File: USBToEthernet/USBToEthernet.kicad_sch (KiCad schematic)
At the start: 14 parts, among them J1 USB_A, J3 RJMG1S8008101BR, U1 LAN7500-ABJZ, U2 NCP1117-3.3_SOT223, U3 93LCxxAxxOT, U4 USBLC6-2SC6, U6 AMS1117-1.2, Y1 25Mhz

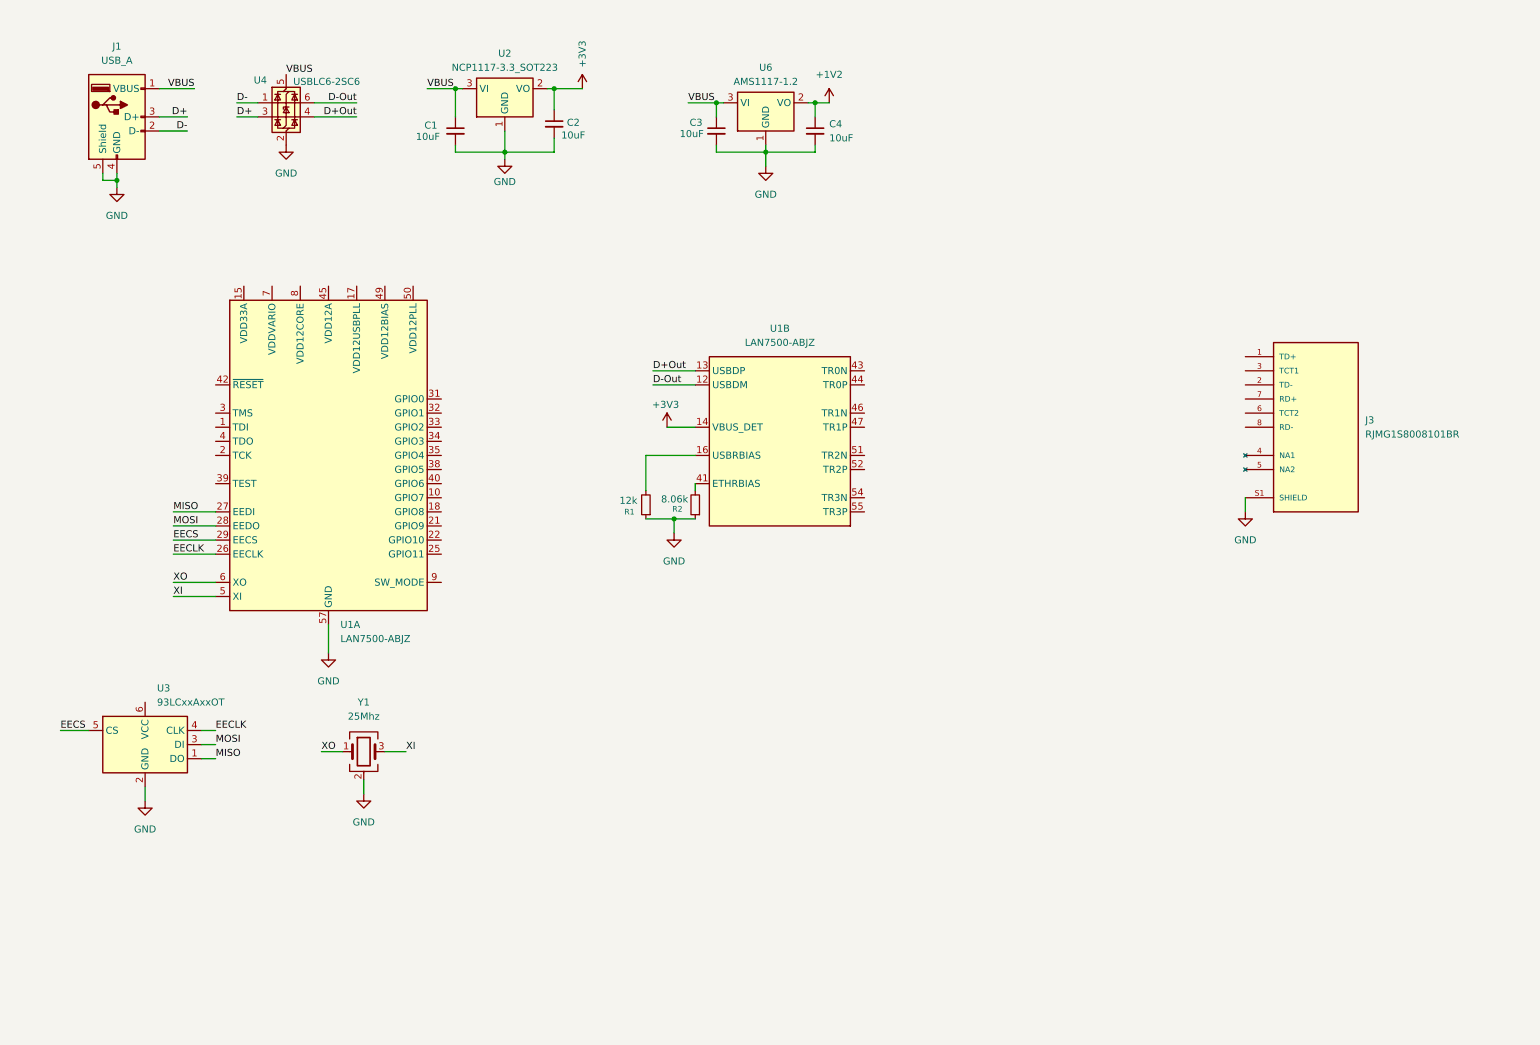
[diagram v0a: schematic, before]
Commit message: Added library for RJ45
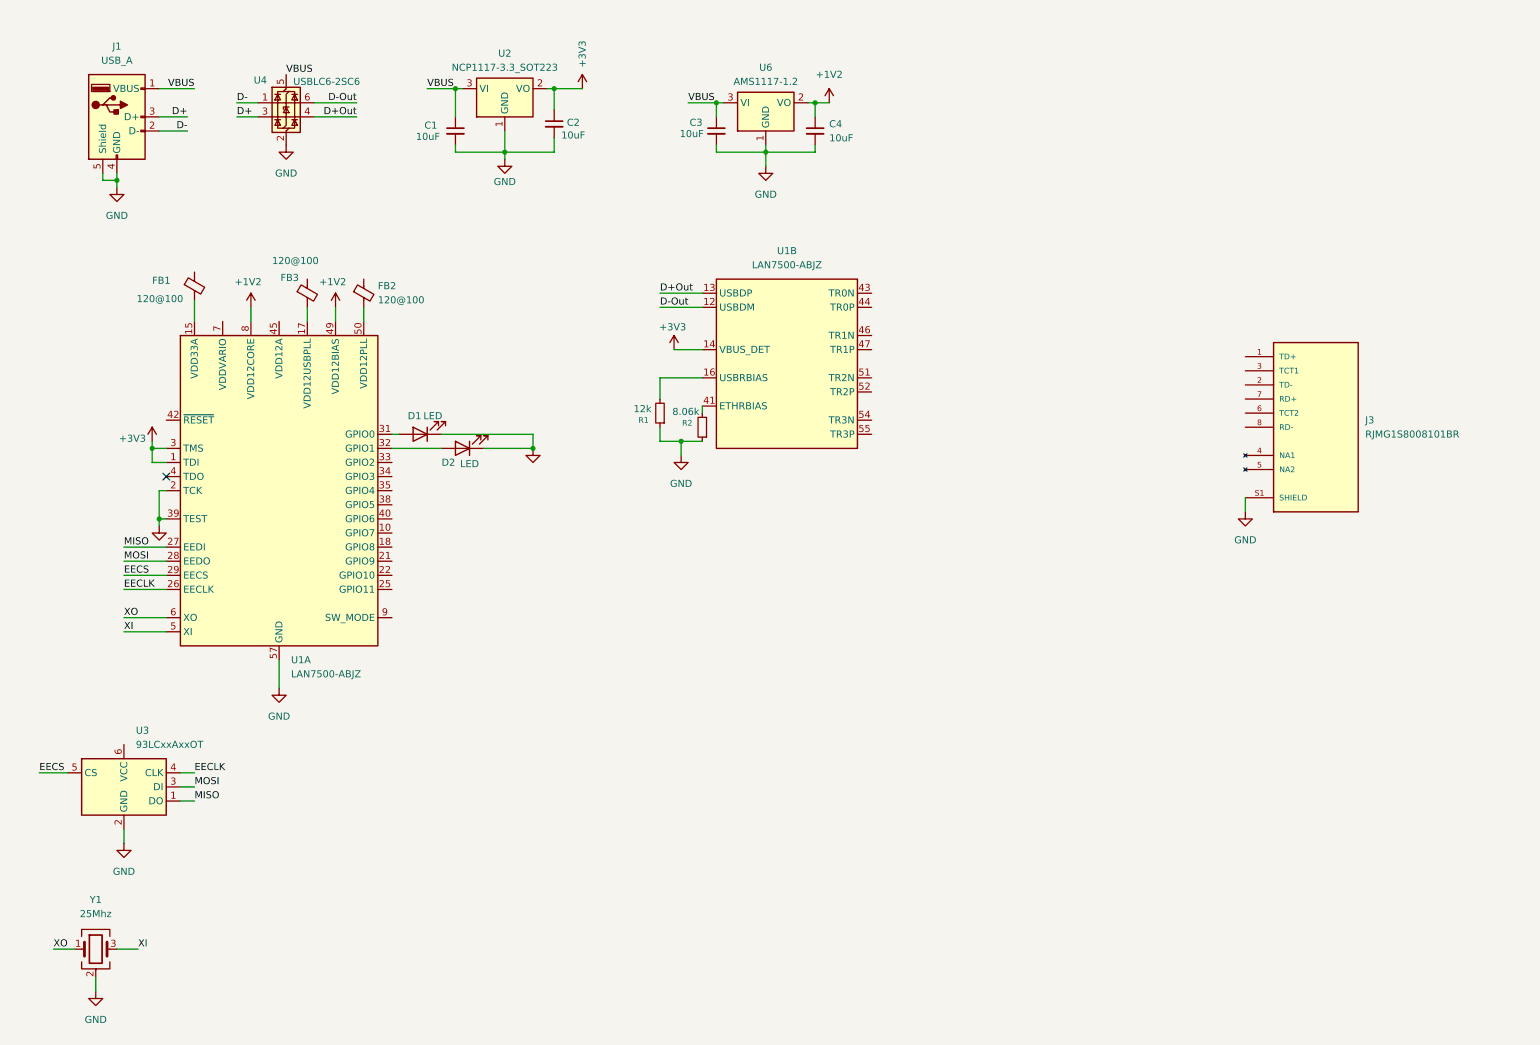
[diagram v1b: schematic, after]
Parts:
- added D1, D2: LED, symbol Device:LED
- added FB1, FB2, FB3: 120@100, symbol Device:FerriteBead_Small
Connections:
- net +1V2: now also U1.11 (VDD12CORE), U1.20 (VDD12CORE), U1.23 (VDD12CORE), U1.30 (VDD12CORE), U1.36 (VDD12CORE), U1.49 (VDD12BIAS), U1.8 (VDD12CORE)
- net +3V3: now also U1.1 (TDI), U1.3 (TMS)
- net GND: now also U1.2 (TCK), U1.39 (TEST), D1.1 (K), D2.1 (K)
- net at U1.15 (VDD33A): now also FB1.2
- net at U1.17 (VDD12USBPLL): now also FB3.2
- net at U1.31 (GPIO0): now also D1.2 (A)
- net at U1.32 (GPIO1): now also D2.2 (A)
- net at U1.50 (VDD12PLL): now also FB2.2
- no-connect marks 0 -> 1
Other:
- moved on the sheet: R1, R2, U1A, U1B, U3, Y1

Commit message: Finished wiring RJ45 and most of LAN7500
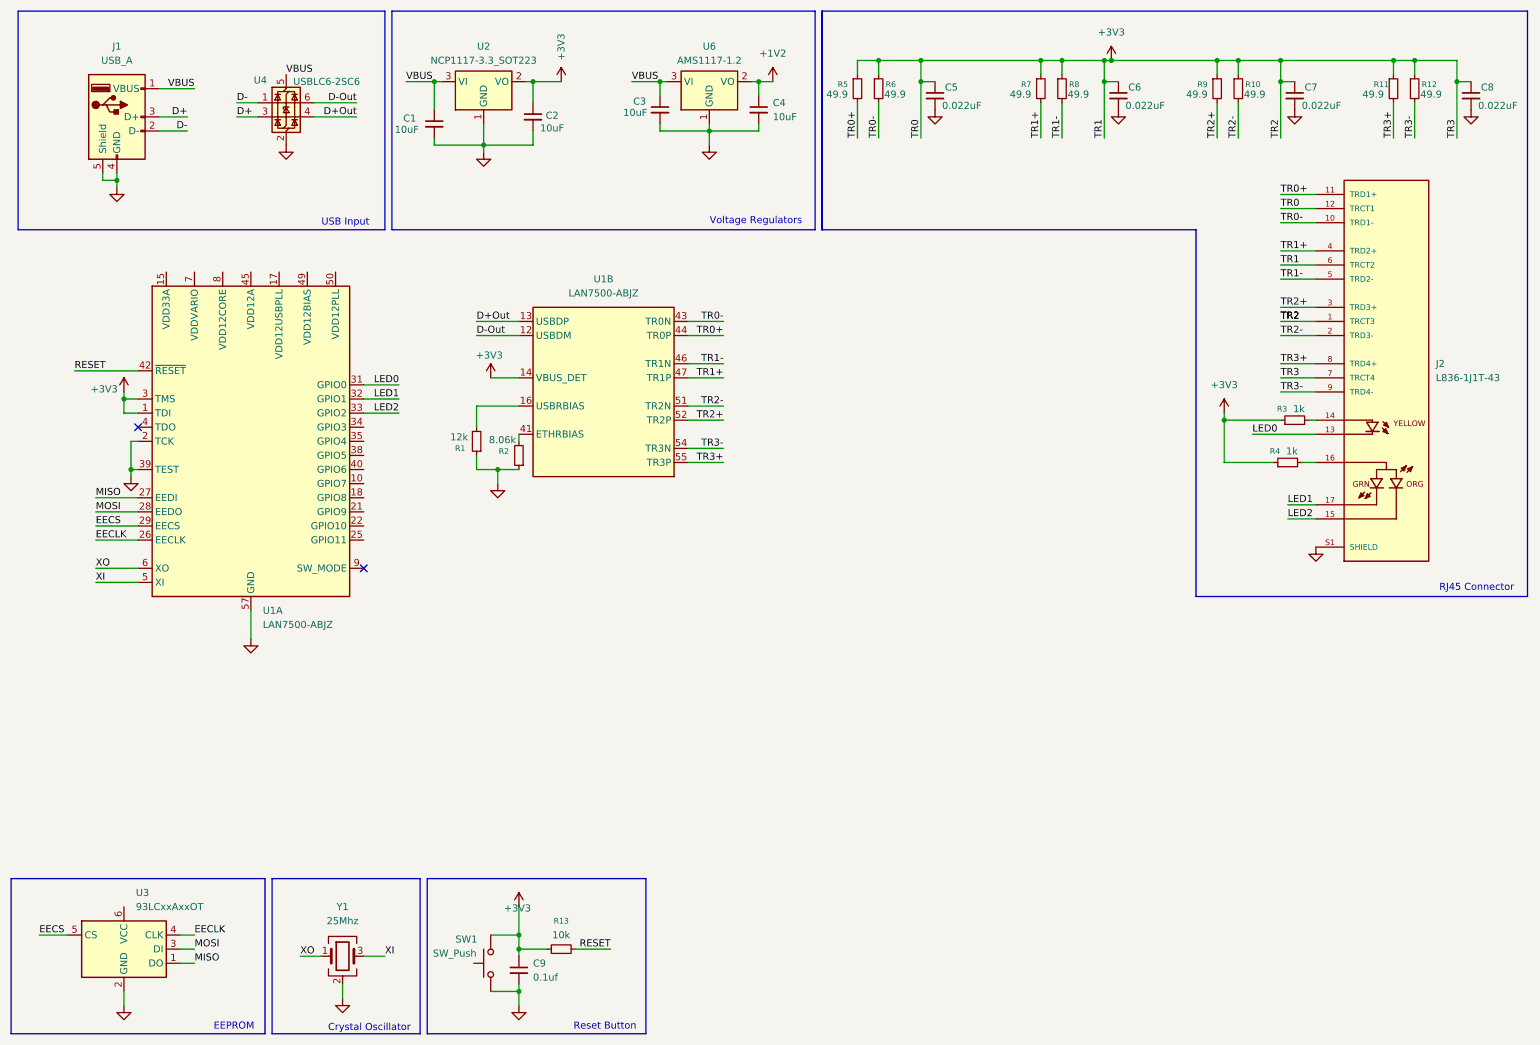
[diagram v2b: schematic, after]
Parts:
- removed D1, D2: LED, symbol Device:LED
- removed FB1, FB2, FB3: 120@100, symbol Device:FerriteBead_Small
- removed J3: RJMG1S8008101BR, RJMG1S8008101BR:AMPHENOL_RJMG1S8008101BR, symbol RJMG1S8008101BR:RJMG1S8008101BR
- added C5, C6, C7, C8: 0.022uF, symbol Device:C_Small
- added C9: 0.1uf, symbol Device:C_Small
- added J2: L836-1J1T-43, L836-1J1T-43:BEL_L836-1J1T-43, symbol L836-1J1T-43:L836-1J1T-43
- added R10, R11, R12, R5, R6, R7, R8, R9: 49.9, Resistor_SMD:R_0201_0603Metric, symbol Device:R_Small
- added R13: 10k, symbol Device:R_Small
- added R3, R4: 1k, symbol Device:R_Small
- added SW1: SW_Push, symbol Switch:SW_Push
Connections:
- net +1V2: no longer U1.11 (VDD12CORE), U1.20 (VDD12CORE), U1.23 (VDD12CORE), U1.30 (VDD12CORE), U1.36 (VDD12CORE), U1.49 (VDD12BIAS), U1.8 (VDD12CORE)
- net +3V3: now also C5.1, C6.1, C7.1, C8.1, C9.1, J2.1 (TRCT3), J2.12 (TRCT1), J2.6 (TRCT2), J2.7 (TRCT4), R10.1, R11.1, R12.1, R13.1, R3.1, R4.1, R5.1, R6.1, R7.1, R8.1, R9.1, SW1.2
- net GND: now also C5.2, C6.2, C7.2, C8.2, C9.2, J2.S1 (SHIELD), J2.S2 (SHIELD), SW1.1
- net TR0-: now reaches U1.43 (TR0N)
- net TR0-: now also J2.10 (TRD1-), R6.2
- net TR0+: now reaches U1.44 (TR0P)
- net TR0+: now also J2.11 (TRD1+), R5.2
- net TR1-: now reaches U1.46 (TR1N)
- net TR1-: now also J2.5 (TRD2-), R8.2
- net TR1+: now reaches U1.47 (TR1P)
- net TR1+: now also J2.4 (TRD2+), R7.2
- net TR2-: now reaches U1.51 (TR2N)
- net TR2-: now also J2.2 (TRD3-), R10.2
- net TR2+: now reaches U1.52 (TR2P)
- net TR2+: now also J2.3 (TRD3+), R9.2
- net TR3-: now reaches U1.54 (TR3N)
- net TR3-: now also J2.9 (TRD4-), R12.2
- net TR3+: now reaches U1.55 (TR3P)
- net TR3+: now also J2.8 (TRD4+), R11.2
- net LED0: now reaches U1.31 (GPIO0)
- net LED0: now also J2.13
- net LED1: now reaches U1.32 (GPIO1)
- net LED1: now also J2.17
- net LED2: now reaches U1.33 (GPIO2)
- net LED2: now also J2.15
- net RESET: now reaches U1.42 (~{RESET})
- net RESET: now also R13.2
- new net: U1.11 (VDD12CORE), U1.20 (VDD12CORE), U1.23 (VDD12CORE), U1.30 (VDD12CORE), U1.36 (VDD12CORE), U1.8 (VDD12CORE)
- new net: J2.14, R3.2
- new net: J2.16, R4.2
- no-connect marks 1 -> 2
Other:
- note added: "Crystal Oscillator"
- note added: "EEPROM"
- note added: "RJ45 Connector"
- note added: "Reset Button"
- note added: "USB Input"
- note added: "Voltage Regulators"
- moved on the sheet: C1, C2, C3, C4, R1, R2, U1A, U1B, U2, U3, U6, Y1

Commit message: Finished schematic
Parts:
- added C10, C11, C12, C13, C14, C15, C16, C17, C18, C20, C21, C22, C23, C24, C25: 1uF, Capacitor_SMD:C_0603_1608Metric, symbol Device:C_Small
- added C19: 100nF, Capacitor_SMD:C_0603_1608Metric, symbol Device:C_Small
- added D1: PTVS10VZ1USK, Diode_SMD:Nexperia_DSN1608-2_1.6x0.8mm, symbol Diode:PTVS10VZ1USK
- added FB1, FB2, FB3, FB4, FB5: 120@100, Inductor_SMD:L_0603_1608Metric, symbol Device:FerriteBead_Small
- C1, C2, C3, C4, C5, C6, C7, C8: footprint (none) -> Capacitor_SMD:C_0603_1608Metric
- C9: value 0.1uf -> 100nF; footprint (none) -> Capacitor_SMD:C_0603_1608Metric
- J1: footprint (none) -> USB_AP_S_RA_SMT:CONN_USB-AP-S-RA-SMT_ADM
- R1, R13, R2, R3, R4: footprint (none) -> Resistor_SMD:R_0603_1608Metric
- SW1: footprint (none) -> Button_Switch_SMD:SW_SPST_PTS645Sx43SMTR92
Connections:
- net +1V2: now also U1.11 (VDD12CORE), U1.20 (VDD12CORE), U1.23 (VDD12CORE), U1.30 (VDD12CORE), U1.36 (VDD12CORE), U1.49 (VDD12BIAS), U1.8 (VDD12CORE), C10.1, C11.1, C12.1, C13.1, C14.1, C15.1, C16.1, FB1.1, FB2.1, FB5.1
- net +3V3: now also U1.19 (VDDVARIO), U1.24 (VDDVARIO), U1.37 (VDDVARIO), U1.7 (VDDVARIO), U3.6 (VCC), C21.1, C22.1, C23.1, C24.1, FB3.1, FB4.1; no longer C5.1, C6.1, C7.1, C8.1, J2.1 (TRCT3), J2.12 (TRCT1), J2.6 (TRCT2), J2.7 (TRCT4), R10.1, R11.1, R12.1, R5.1, R6.1, R7.1, R8.1, R9.1
- net GND: now also C10.2, C11.2, C12.2, C13.2, C14.2, C15.2, C16.2, C17.2, C18.2, C19.2, C20.2, C21.2, C22.2, C23.2, C24.2, C25.2
- net VBUS: now also C19.1, D1.1 (K); no longer J1.1 (VBUS)
- net VDD33A: now reaches U1.15 (VDD33A)
- net VDD33A: now also C20.1, FB3.2
- net VDD12USBPLL: now reaches U1.17 (VDD12USBPLL)
- net VDD12USBPLL: now also C18.1, FB2.2
- net VDD12A: now reaches U1.45 (VDD12A), U1.48 (VDD12A), U1.53 (VDD12A), U1.56 (VDD12A)
- net VDD12A: now also C25.1, FB5.2
- net VDD12PLL: now reaches U1.50 (VDD12PLL)
- net VDD12PLL: now also C17.1, FB1.2
- new net: D1.2 (A), J1.1 (VBUS)
- new net TR0: C5.1, C6.1, C7.1, C8.1, FB4.2, J2.1 (TRCT3), J2.12 (TRCT1), J2.6 (TRCT2), J2.7 (TRCT4), R10.1, R11.1, R12.1, R5.1, R6.1, R7.1, R8.1, R9.1
- no-connect marks 2 -> 11
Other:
- note added: "LAN7500 1V2 Power"
- note added: "LAN7500 3V3 Power"
- note added: "LAN7500 Chip"
- moved on the sheet: C1, C2, C3, C4, C5, C6, C7, C8, J1, R1, R10, R11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

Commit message: misc. changes
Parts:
- removed D1: PTVS10VZ1USK, Diode_SMD:Nexperia_DSN1608-2_1.6x0.8mm, symbol Diode:PTVS10VZ1USK
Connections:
- net VBUS: now also J1.1 (VBUS)
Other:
- moved on the sheet: FB4
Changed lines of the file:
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@@
 	)
 	(junction
+		(at 29.21 26.67)
+		(diameter 0)
+		(color 0 0 0 0)
+	)
+	(junction
 		(at 46.99 158.75)
 		(diameter 0)
@@
 	)
 	(junction
-		(at 209.55 25.4)
-		(diameter 0)
-		(color 0 0 0 0)
-	)
-	(junction
 		(at 182.88 72.39)
 		(diameter 0)
@@
 	)
 	(junction
+		(at 218.44 25.4)
+		(diameter 0)
+		(color 0 0 0 0)
+	)
+	(junction
 		(at 182.88 80.01)
 		(diameter 0)
@@
 	(wire
 		(pts
+			(xy 25.4 26.67) (xy 29.21 26.67)
+		)
+		(stroke
+			(width 0)
+			(type default)
+		)
+	)
+	(wire
+		(pts
 			(xy 149.86 73.66) (xy 153.67 73.66)
 		)
@@
 	(wire
 		(pts
-			(xy 208.28 25.4) (xy 209.55 25.4)
+			(xy 208.28 25.4) (xy 218.44 25.4)
 		)
 		(stroke
@@
 		)
 	)
+	(wire
+		(pts
+			(xy 29.21 26.67) (xy 41.91 26.67)
+		)
+		(stroke
+			(width 0)
+			(type default)
+		)
+	)
 	(polyline
 		(pts
@@
 	(wire
 		(pts
-			(xy 240.03 76.2) (xy 246.38 76.2)
+			(xy 218.44 25.4) (xy 228.6 25.4)
 		)
 		(stroke
@@
 	(wire
 		(pts
-			(xy 107.95 27.94) (xy 113.03 27.94)
+			(xy 240.03 76.2) (xy 246.38 76.2)
 		)
 		(stroke
@@
 	(wire
 		(pts
-			(xy 129.54 107.95) (xy 135.89 107.95)
+			(xy 107.95 27.94) (xy 113.03 27.94)
 		)
 		(stroke
@@
 	(wire
 		(pts
-			(xy 29.21 26.67) (xy 31.75 26.67)
+			(xy 129.54 107.95) (xy 135.89 107.95)
 		)
 		(stroke
@@
 	(wire
 		(pts
-			(xy 209.55 16.51) (xy 209.55 17.78)
+			(xy 218.44 16.51) (xy 218.44 17.78)
 		)
 		(stroke
@@
 	(wire
 		(pts
-			(xy 39.37 26.67) (xy 45.72 26.67)
-		)
-		(stroke
-			(width 0)
-			(type default)
-		)
-	)
-	(wire
-		(pts
 			(xy 182.88 72.39) (xy 182.88 73.66)
 		)
@@
 	(wire
 		(pts
-			(xy 209.55 25.4) (xy 228.6 25.4)
-		)
-		(stroke
-			(width 0)
-			(type default)
-		)
-	)
-	(wire
-		(pts
 			(xy 129.54 87.63) (xy 135.89 87.63)
 		)
@@
 	(wire
 		(pts
-			(xy 209.55 22.86) (xy 209.55 25.4)
+			(xy 218.44 22.86) (xy 218.44 25.4)
 		)
 		(stroke
@@
 	)
 	(label "VBUS"
-		(at 44.45 26.67 180)
+		(at 40.64 26.67 180)
 		(effects
 			(font
@@
 	(symbol
 		(lib_id "Device:FerriteBead_Small")
-		(at 209.55 20.32 0)
+		(at 218.44 20.32 0)
 		(unit 1)
 		(exclude_from_sim no)
@@
 		(dnp no)
 		(property "Reference" "FB4"
-			(at 211.582 19.304 0)
+			(at 220.472 19.304 0)
 			(effects
 				(font
@@
 		)
 		(property "Value" "120@100"
-			(at 211.582 21.59 0)
+			(at 220.472 21.59 0)
 			(effects
 				(font
@@
 		)
 		(property "Footprint" "Inductor_SMD:L_0603_1608Metric"
-			(at 207.772 20.32 90)
+			(at 216.662 20.32 90)
 			(effects
 				(font
@@
 		)
 		(property "Datasheet" "~"
-			(at 209.55 20.32 0)
+			(at 218.44 20.32 0)
 			(effects
 				(font
@@
 		)
 		(property "Description" "Ferrite bead, small symbol"
-			(at 209.55 20.32 0)
+			(at 218.44 20.32 0)
 			(effects
 				(font
@@
 	(symbol
 		(lib_id "power:PWR_FLAG")
-		(at 45.72 26.67 0)
+		(at 41.91 26.67 0)
 		(unit 1)
 		(exclude_from_sim no)
@@
 		(dnp no)
 		(property "Reference" "#FLG08"
-			(at 45.72 24.765 0)
+			(at 41.91 24.765 0)
 			(effects
 				(font
@@
 		)
 		(property "Value" "PWR_FLAG"
-			(at 51.816 25.146 0)
+			(at 48.006 25.146 0)
 			(effects
 				(font
@@
 		)
 		(property "Footprint" ""
-			(at 45.72 26.67 0)
+			(at 41.91 26.67 0)
 			(effects
 				(font
@@
 		)
 		(property "Datasheet" "~"
-			(at 45.72 26.67 0)
+			(at 41.91 26.67 0)
 			(effects
 				(font
@@
 		)
 		(property "Description" "Special symbol for telling ERC where power comes from"
-			(at 45.72 26.67 0)
+			(at 41.91 26.67 0)
 			(effects
 				(font
@@
 	)
 	(symbol
-		(lib_id "Diode:PTVS10VZ1USK")
-		(at 35.56 26.67 180)
-		(unit 1)
-		(exclude_from_sim no)
-		(in_bom yes)
-		(on_board yes)
-		(dnp no)
-		(fields_autoplaced yes)
-		(property "Reference" "D1"
-			(at 35.56 20.32 0)
-			(effects
-				(font
-					(size 1.27 1.27)
-				)
-			)
-		)
-		(property "Value" "PTVS10VZ1USK"
-			(at 35.56 22.86 0)
-			(effects
-				(font
-					(size 1.27 1.27)
-				)
-			)
-		)
-		(property "Footprint" "Diode_SMD:Nexperia_DSN1608-2_1.6x0.8mm"
-			(at 35.56 22.225 0)
-			(effects
-				(font
-					(size 1.27 1.27)
-				)
-				(hide yes)
-			)
-		)
-		(property "Datasheet" "https://assets.nexperia.com/documents/data-sheet/PTVS10VZ1USK.pdf"
-			(at 35.56 26.67 0)
-			(effects
-				(font
-					(size 1.27 1.27)
-				)
-				(hide yes)
-			)
-		)
-		(property "Description" "10V, 2000W TVS unidirectional diode, DSN1608-2"
-			(at 35.56 26.67 0)
-			(effects
-				(font
-					(size 1.27 1.27)
-				)
-				(hide yes)
-			)
-		)
-		(pin "2"
-		)
-		(pin "1"
-		)
-		(instances
-			(project ""
-				(path "/e2f4c3a6-d848-4365-9cff-800700e3d63d"
-					(reference "D1")
-					(unit 1)
-				)
-			)
-		)
-	)
-	(symbol
 		(lib_id "Device:C_Small")
 		(at 90.17 35.56 0)
@@
 	(symbol
 		(lib_id "power:+3V3")
-		(at 209.55 16.51 0)
+		(at 218.44 16.51 0)
 		(unit 1)
 		(exclude_from_sim no)
@@
 		(dnp no)
 		(property "Reference" "#PWR09"
-			(at 209.55 20.32 0)
+			(at 218.44 20.32 0)
 			(effects
 				(font
@@
 		)
 		(property "Value" "+3V3"
-			(at 213.36 14.732 0)
+			(at 222.25 14.732 0)
 			(effects
 				(font
@@
 		)
 		(property "Footprint" ""
-			(at 209.55 16.51 0)
+			(at 218.44 16.51 0)
 			(effects
 				(font
@@
 		)
 		(property "Datasheet" ""
-			(at 209.55 16.51 0)
+			(at 218.44 16.51 0)
 			(effects
 				(font
@@
 		)
 		(property "Description" "Power symbol creates a global label with name \"+3V3\""
-			(at 209.55 16.51 0)
+			(at 218.44 16.51 0)
 			(effects
 				(font
